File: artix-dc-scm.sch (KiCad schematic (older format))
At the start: 0 parts

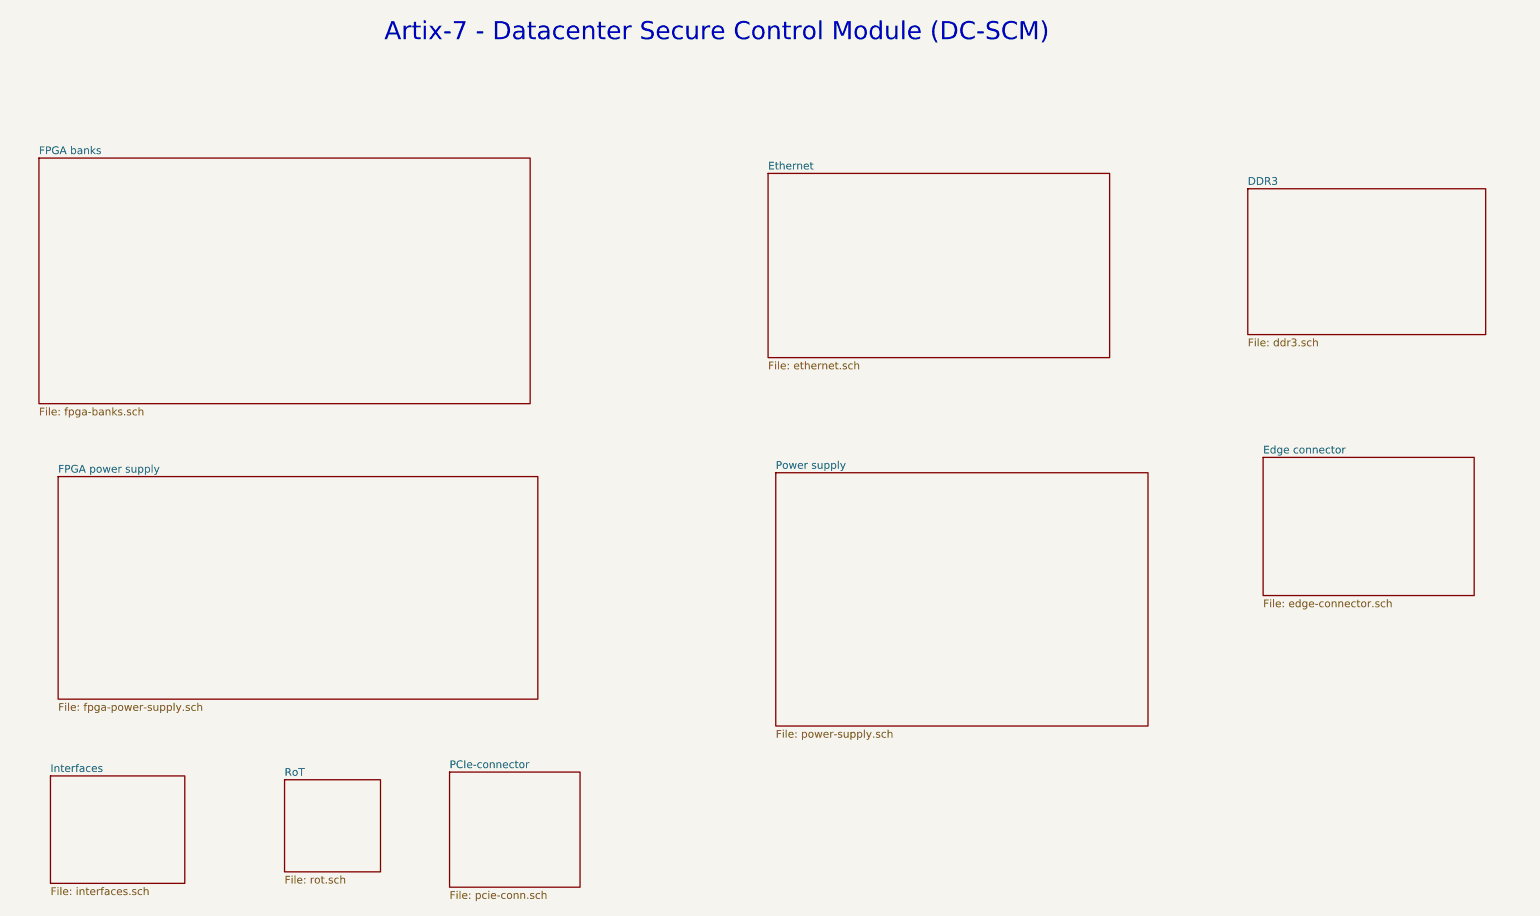
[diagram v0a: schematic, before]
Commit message: Neatened main sheet
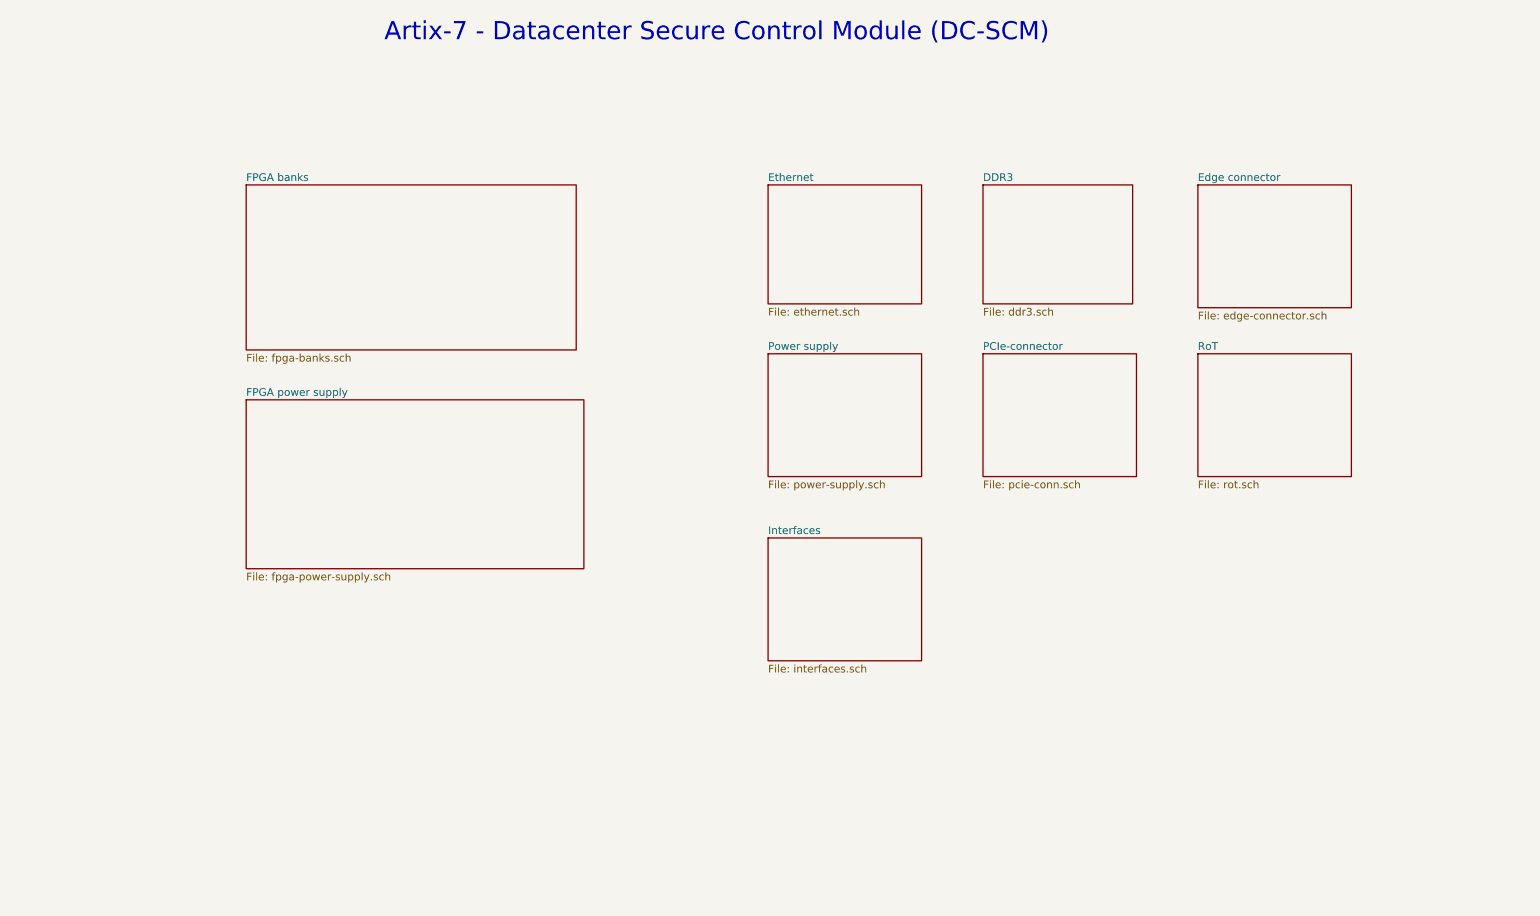
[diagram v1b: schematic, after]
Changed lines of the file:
@@
 Artix-7 - Datacenter Secure Control Module (DC-SCM)
 $Sheet
-S 1150 1725 3200 1600
+S 2500 1900 2150 1075
 U 5FC6B687
 F0 "FPGA banks" 50
@@
 $EndSheet
 $Sheet
-S 1275 3800 3125 1450
+S 2500 3300 2200 1100
 U 626D078D
 F0 "FPGA power supply" 50
@@
 $EndSheet
 $Sheet
-S 5900 1825 2225 1200
-U 60570C04
-F0 "Ethernet" 50
-F1 "ethernet.sch" 50
-$EndSheet
-$Sheet
-S 5950 3775 2425 1650
+S 5900 3000 1000 800
 U 5FCA4661
 F0 "Power supply" 50
@@
 $EndSheet
 $Sheet
-S 9025 1925 1550 950
+S 7300 1900 975  775
 U 5FD8EBC2
 F0 "DDR3" 50
@@
 $EndSheet
 $Sheet
-S 1225 5750 875  700
+S 5900 4200 1000 800
 U 614223A1
 F0 "Interfaces" 50
@@
 $EndSheet
 $Sheet
-S 9125 3675 1375 900
+S 8700 1900 1000 800
 U 625AEC25
 F0 "Edge connector" 50
@@
 $EndSheet
 $Sheet
-S 2750 5775 625  600
+S 8700 3000 1000 800
 U 624C566F
 F0 "RoT" 50
@@
 $EndSheet
 $Sheet
-S 3825 5725 850  750
+S 7300 3000 1000 800
 U 5FD17EF1
 F0 "PCIe-connector" 50
 F1 "pcie-conn.sch" 50
 $EndSheet
+$Sheet
+S 5900 1900 1000 775
+U 60570C04
+F0 "Ethernet" 50
+F1 "ethernet.sch" 50
+$EndSheet
 $EndSCHEMATC

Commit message: Update after designator unification
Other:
- note added: "Artix - Datacenter Secure Control Module (DC-SCM)"
- note removed: "Artix-7 - Datacenter Secure Control Module (DC-SCM)"
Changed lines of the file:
@@
 $EndDescr
 Text Notes 3400 975  0    118  ~ 0
-Artix-7 - Datacenter Secure Control Module (DC-SCM)
+Artix - Datacenter Secure Control Module (DC-SCM)
 $Sheet
-S 2500 1900 2150 1075
-U 5FC6B687
+S 2375 4750 1875 1025
+U 5FD86C51
+F0 "FPGA power supply" 50
+F1 "fpga-power-supply.sch" 50
+$EndSheet
+$Sheet
+S 4950 4750 1900 1075
+U 5FD86CE4
 F0 "FPGA banks" 50
 F1 "fpga-banks.sch" 50
 $EndSheet
 $Sheet
-S 2500 3300 2200 1100
-U 626D078D
-F0 "FPGA power supply" 50
-F1 "fpga-power-supply.sch" 50
-$EndSheet
-$Sheet
-S 5900 3000 1000 800
-U 5FCA4661
+S 9725 2650 1125 750
+U 5FD86BEB
 F0 "Power supply" 50
 F1 "power-supply.sch" 50
 $EndSheet
 $Sheet
-S 7300 1900 975  775
+S 8150 2650 1025 725
 U 5FD8EBC2
 F0 "DDR3" 50
@@
 $EndSheet
 $Sheet
-S 5900 4200 1000 800
+S 6550 2675 1100 750
 U 614223A1
 F0 "Interfaces" 50
@@
 $EndSheet
 $Sheet
-S 8700 1900 1000 800
+S 5200 2600 1150 725
 U 625AEC25
 F0 "Edge connector" 50
@@
 $EndSheet
 $Sheet
-S 8700 3000 1000 800
+S 3900 2625 1100 750
 U 624C566F
 F0 "RoT" 50
@@
 $EndSheet
 $Sheet
-S 7300 3000 1000 800
+S 2425 2625 1125 750
 U 5FD17EF1
 F0 "PCIe-connector" 50
@@
 $EndSheet
 $Sheet
-S 5900 1900 1000 775
+S 975  2625 1000 725
 U 60570C04
 F0 "Ethernet" 50
